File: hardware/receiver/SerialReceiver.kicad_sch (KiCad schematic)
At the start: 20 parts

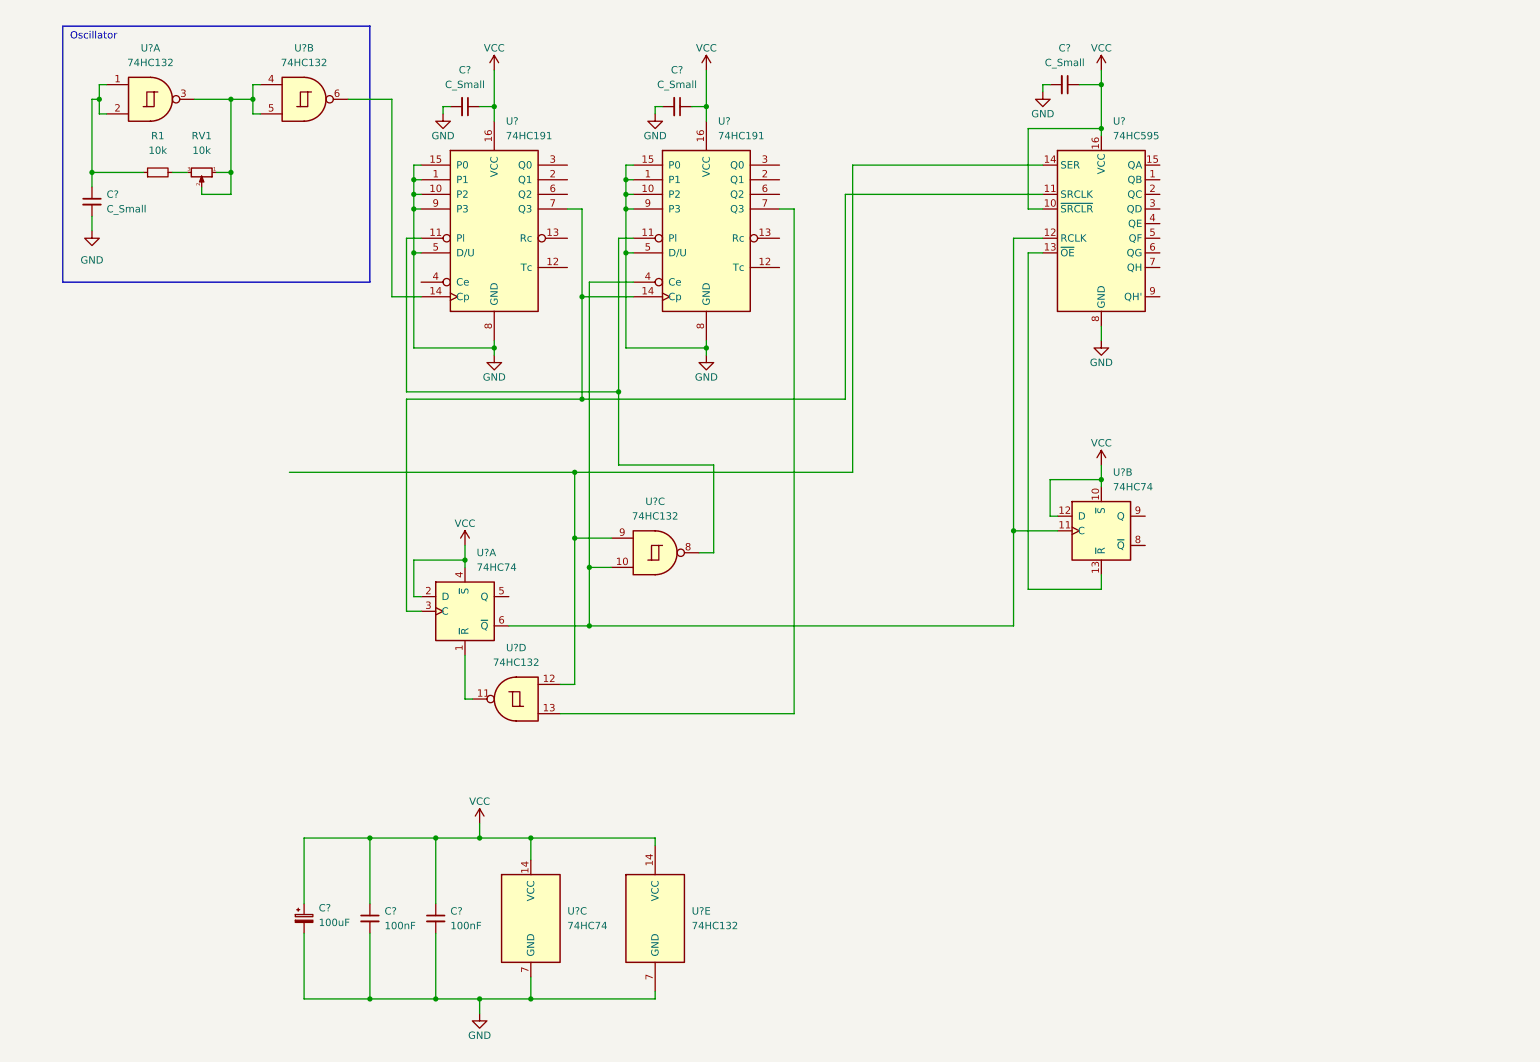
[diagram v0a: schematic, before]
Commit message: Continued the design of the receiver.
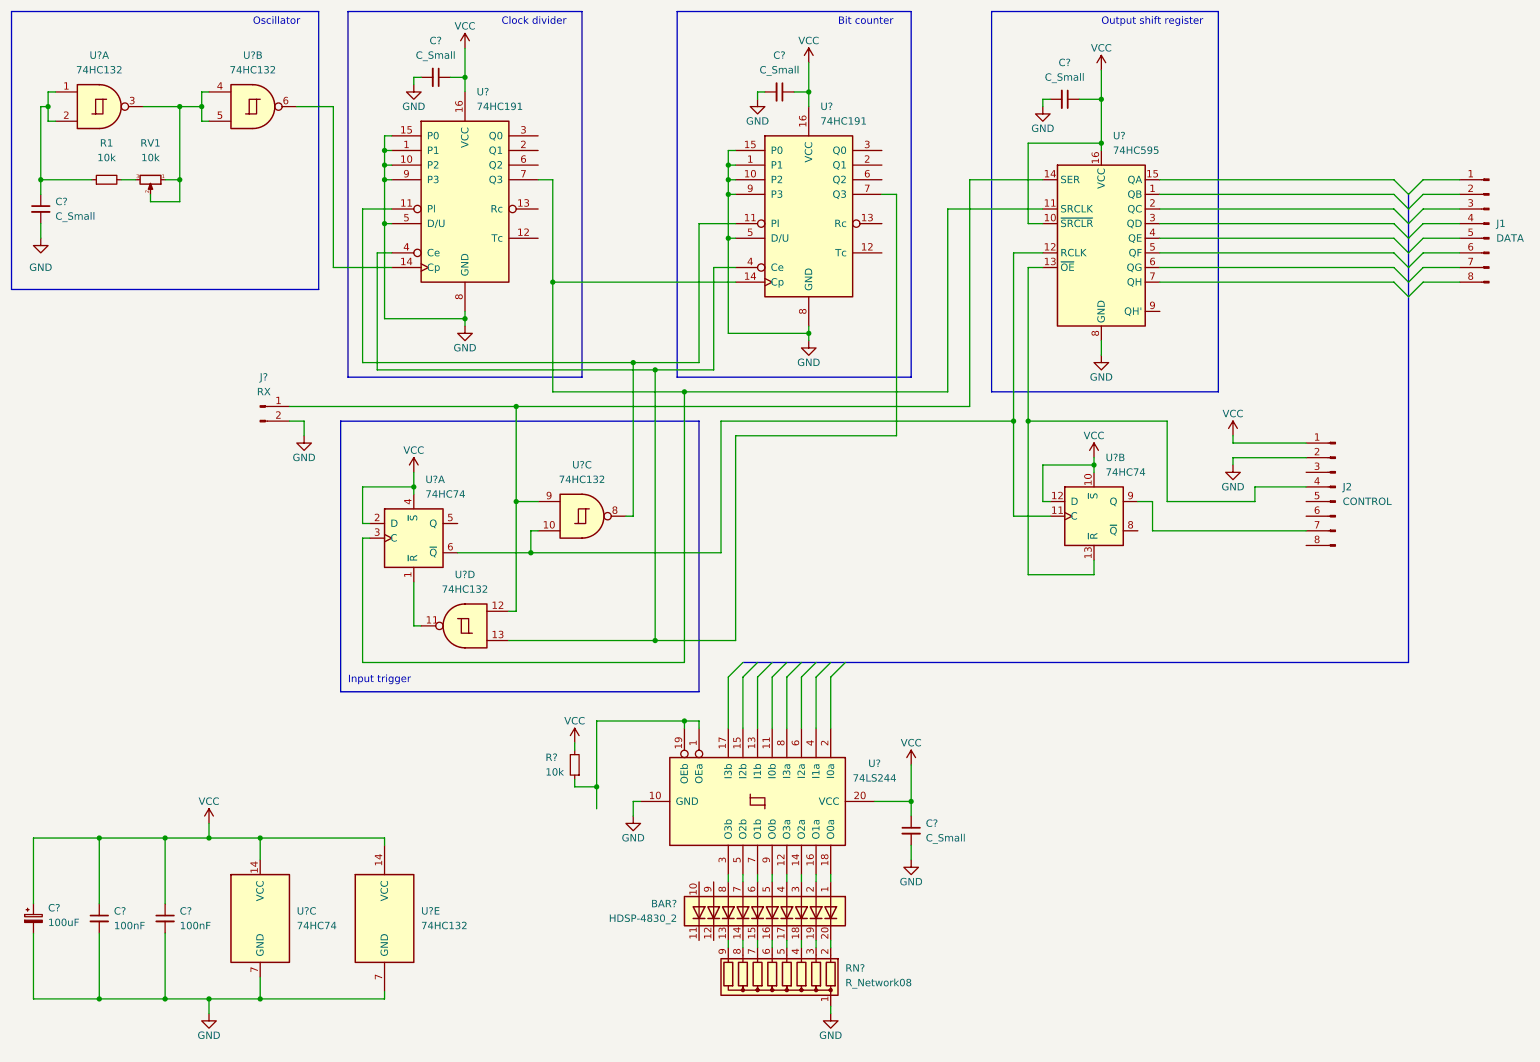
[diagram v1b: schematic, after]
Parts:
- added BAR?: HDSP-4830_2, Display:HDSP-4830, symbol LED:HDSP-4830_2
- added C?: C_Small, symbol Device:C_Small
- added J1: DATA, symbol Connector:Conn_01x08_Male
- added J2: CONTROL, symbol Connector:Conn_01x08_Male
- added J?: RX, symbol Connector:Conn_01x02_Male
- added R?: 10k, symbol Device:R_Small
- added RN?: R_Network08, Resistor_THT:R_Array_SIP9, symbol Device:R_Network08
- added U?: 74LS244, symbol 74xx:74LS244
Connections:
- net GND: now also C?.2, J2.2 (Pin_2), J?.2 (Pin_2), RN?.1 (common), U?.10 (GND)
- net VCC: now also C?.1, J2.1 (Pin_1), R?.2, U?.20 (VCC)
- net at U?.4 (Ce): now also U?.13, U?.4 (Ce), U?.7 (Q3)
- net at U?.10, U?.11 (C), U?.12 (RCLK)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: no longer U?.4 (Ce)
- net at U?.13 (~{OE}), U?.13 (~{R}): now also J2.4 (Pin_4)
- net at U?.9 (Q): now also J2.7 (Pin_7)
- net at U?.12, U?.14 (SER), U?.9: now also J?.1 (Pin_1)
- new net: BAR?.1 (A), U?.18 (O0a)
- new net: BAR?.13 (K), RN?.9 (R8)
- new net: BAR?.14 (K), RN?.8 (R7)
- new net: BAR?.15 (K), RN?.7 (R6)
- new net: BAR?.16 (K), RN?.6 (R5)
- new net: BAR?.17 (K), RN?.5 (R4)
- new net: BAR?.18 (K), RN?.4 (R3)
- new net: BAR?.19 (K), RN?.3 (R2)
- new net: BAR?.2 (A), U?.16 (O1a)
- new net: BAR?.20 (K), RN?.2 (R1)
- new net: BAR?.3 (A), U?.14 (O2a)
- new net: BAR?.4 (A), U?.12 (O3a)
- new net: BAR?.5 (A), U?.9 (O0b)
- new net: BAR?.6 (A), U?.7 (O1b)
- new net: BAR?.7 (A), U?.5 (O2b)
- new net: BAR?.8 (A), U?.3 (O3b)
- new net: R?.1, U?.1 (OEa), U?.19 (OEb)
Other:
- note added: "Bit counter"
- note added: "Clock divider"
- note added: "Input trigger"
- note added: "Output shift register"
- moved on the sheet: C?, R1, RV1, U?, U?A, U?B, U?C, U?D, U?E

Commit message: Setting the names and the values of the receiver's components.
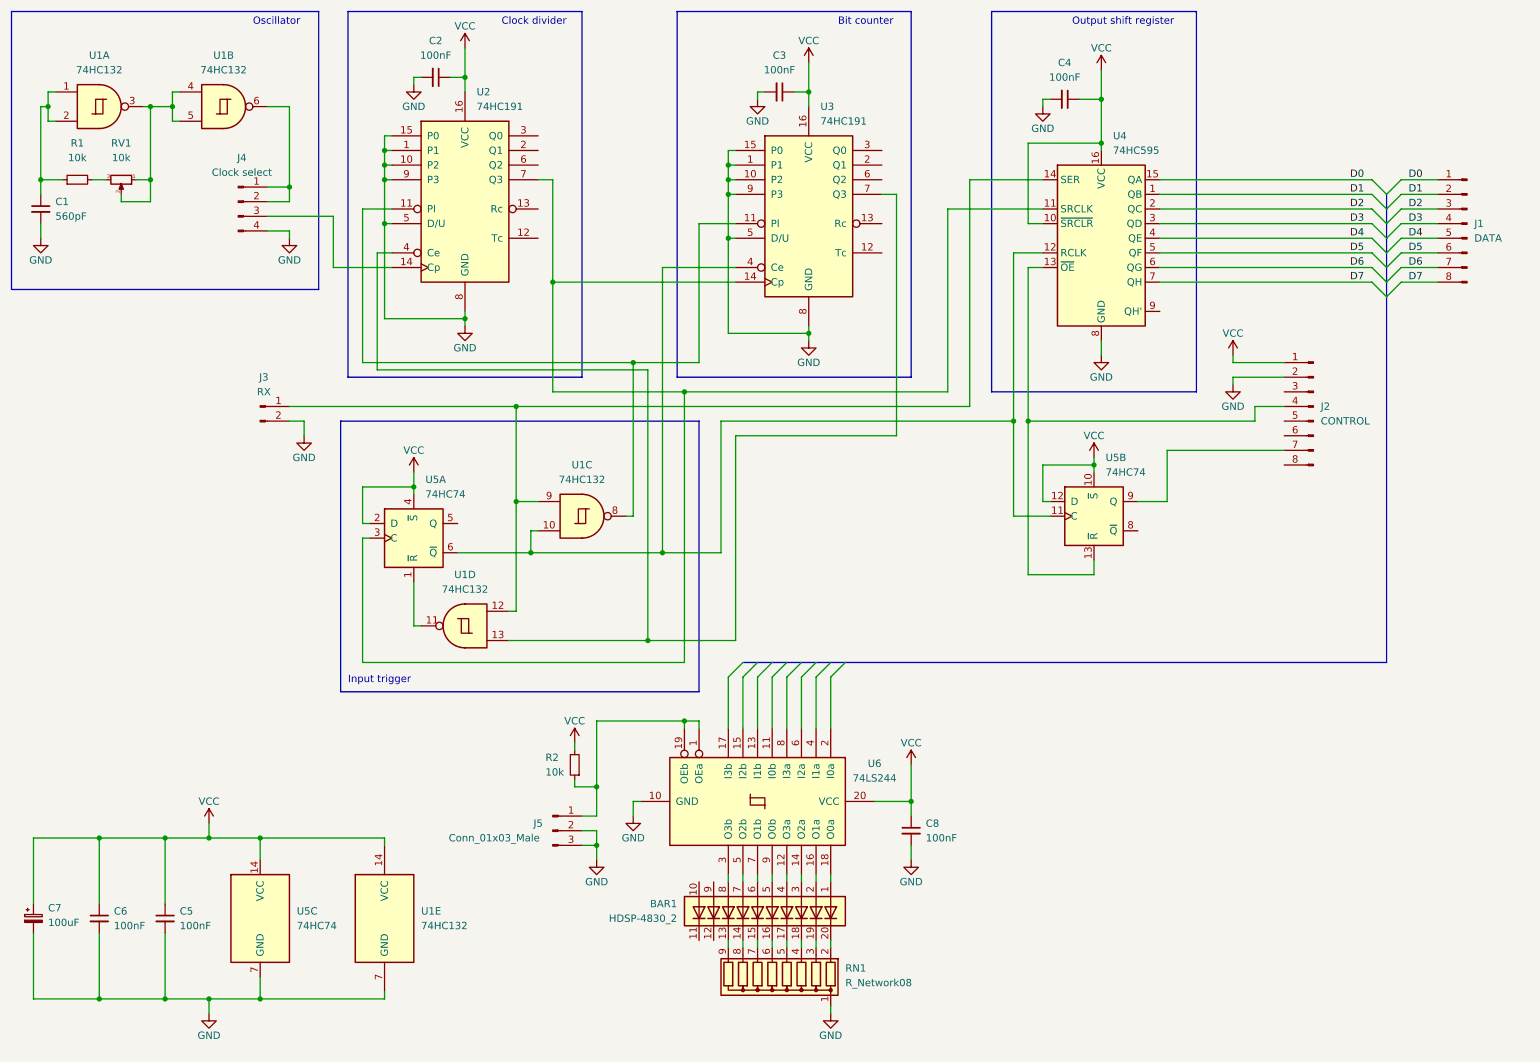
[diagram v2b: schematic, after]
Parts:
- added J4: Clock select, symbol Connector:Conn_01x04_Male
- added J5: Conn_01x03_Male, symbol Connector:Conn_01x03_Male
- C1: renamed from C?; value C_Small -> 560pF
- C2, C3, C4, C8: renamed from C?; value C_Small -> 100nF
- gave numbers to parts that had none: 13
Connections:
- net GND: now also J4.4 (Pin_4), J5.2 (Pin_2), J5.3 (Pin_3)
- net at U1.6: now also J4.1 (Pin_1), J4.2 (Pin_2); no longer U2.14 (Cp)
- net at U1.13, U2.4 (Ce), U3.7 (Q3): no longer U3.4 (Ce)
- net D0: now reaches J1.1 (Pin_1)
- net D0: now also U4.15 (QA)
- net D1: now reaches J1.2 (Pin_2)
- net D1: now also U4.1 (QB)
- net D2: now reaches J1.3 (Pin_3)
- net D2: now also U4.2 (QC)
- net D3: now reaches J1.4 (Pin_4)
- net D3: now also U4.3 (QD)
- net D4: now reaches J1.5 (Pin_5)
- net D4: now also U4.4 (QE)
- net D5: now reaches J1.6 (Pin_6)
- net D5: now also U4.5 (QF)
- net D6: now reaches J1.7 (Pin_7)
- net D6: now also U4.6 (QG)
- net D7: now reaches J1.8 (Pin_8)
- net D7: now also U4.7 (QH)
- net at U1.10, U4.12 (RCLK), U5.11 (C)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: now also U3.4 (Ce)
- net at R2.1, U6.1 (OEa), U6.19 (OEb): now also J5.1 (Pin_1)
- new net: J4.3 (Pin_3), U2.14 (Cp)
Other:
- moved on the sheet: J1, J2, R1, RV1, U1B

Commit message: Starting the PCB design.
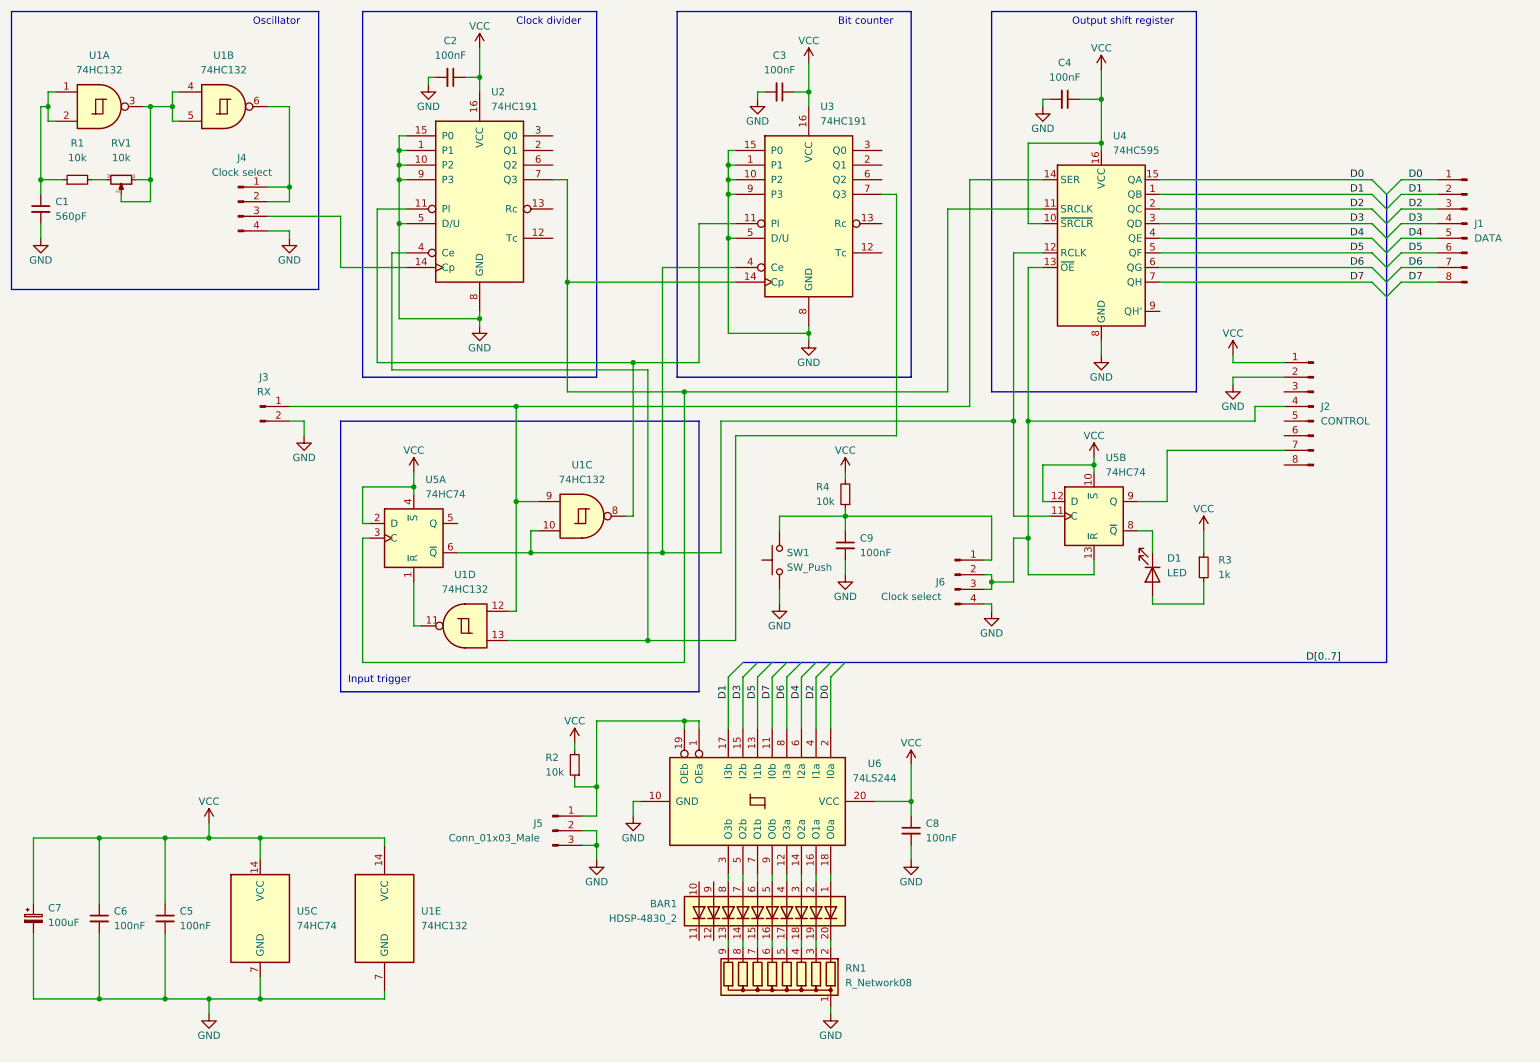
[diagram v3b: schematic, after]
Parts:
- added C9: 100nF, Capacitor_THT:C_Disc_D3.0mm_W2.0mm_P2.50mm, symbol Device:C_Small
- added D1: LED, LED_THT:LED_D3.0mm, symbol Device:LED
- added J6: Clock select, Connector_PinHeader_2.54mm:PinHeader_1x04_P2.54mm_Vertical, symbol Connector:Conn_01x04_Male
- added R3: 1k, Resistor_THT:R_Axial_DIN0207_L6.3mm_D2.5mm_P10.16mm_Horizontal, symbol Device:R_Small
- added R4: 10k, Resistor_THT:R_Axial_DIN0207_L6.3mm_D2.5mm_P10.16mm_Horizontal, symbol Device:R_Small
- added SW1: SW_Push, Button_Switch_THT:SW_PUSH_6mm, symbol Switch:SW_Push
- C1, C2, C3, C4, C5, C6, C8: footprint (none) -> Capacitor_THT:C_Disc_D3.0mm_W2.0mm_P2.50mm
- C7: footprint (none) -> Capacitor_THT:CP_Radial_D6.3mm_P2.50mm
- J1, J2: footprint (none) -> Connector_PinHeader_2.54mm:PinHeader_1x08_P2.54mm_Horizontal
- J3: footprint (none) -> Connector_PinHeader_2.54mm:PinHeader_1x02_P2.54mm_Horizontal
- J4: footprint (none) -> Connector_PinHeader_2.54mm:PinHeader_1x04_P2.54mm_Vertical
- J5: footprint (none) -> Connector_PinHeader_2.54mm:PinHeader_1x03_P2.54mm_Vertical
- R1, R2, RV1: footprint (none) -> Resistor_THT:R_Axial_DIN0207_L6.3mm_D2.5mm_P10.16mm_Horizontal
- U1, U5: footprint (none) -> Package_DIP:DIP-14_W7.62mm
- U2, U3, U4: footprint (none) -> Package_DIP:DIP-16_W7.62mm
- U6: footprint (none) -> Package_DIP:DIP-20_W7.62mm
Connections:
- net D0: now also U6.2 (I0a)
- net D1: now also U6.17 (I3b)
- net D2: now also U6.4 (I1a)
- net D3: now also U6.15 (I2b)
- net D4: now also U6.6 (I2a)
- net D5: now also U6.13 (I1b)
- net D6: now also U6.8 (I3a)
- net D7: now also U6.11 (I0b)
- net GND: now also C9.2, J6.4 (Pin_4), SW1.1
- net VCC: now also R3.1, R4.2
- net at J2.4 (Pin_4), U4.13 (~{OE}), U5.13 (~{R}): now also J6.2 (Pin_2), J6.3 (Pin_3)
- net at U5.8 (~{Q}): now also D1.1 (K)
- new net: C9.1, J6.1 (Pin_1), R4.1, SW1.2
- new net: D1.2 (A), R3.2
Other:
- moved on the sheet: C2, U2
